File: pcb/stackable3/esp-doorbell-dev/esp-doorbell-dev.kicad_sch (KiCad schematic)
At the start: 26 parts, among them J1 JST XH, J2 Screw_Terminal_01x02, J3 JST XH/PH, J4 JST PH, Q1 BSS84, Q2 BSS84, Q3 BSS84, Q4 2N7002DW, Q5 BSS138, U1 WS2811F, U2 G3MB-202P-5VDC

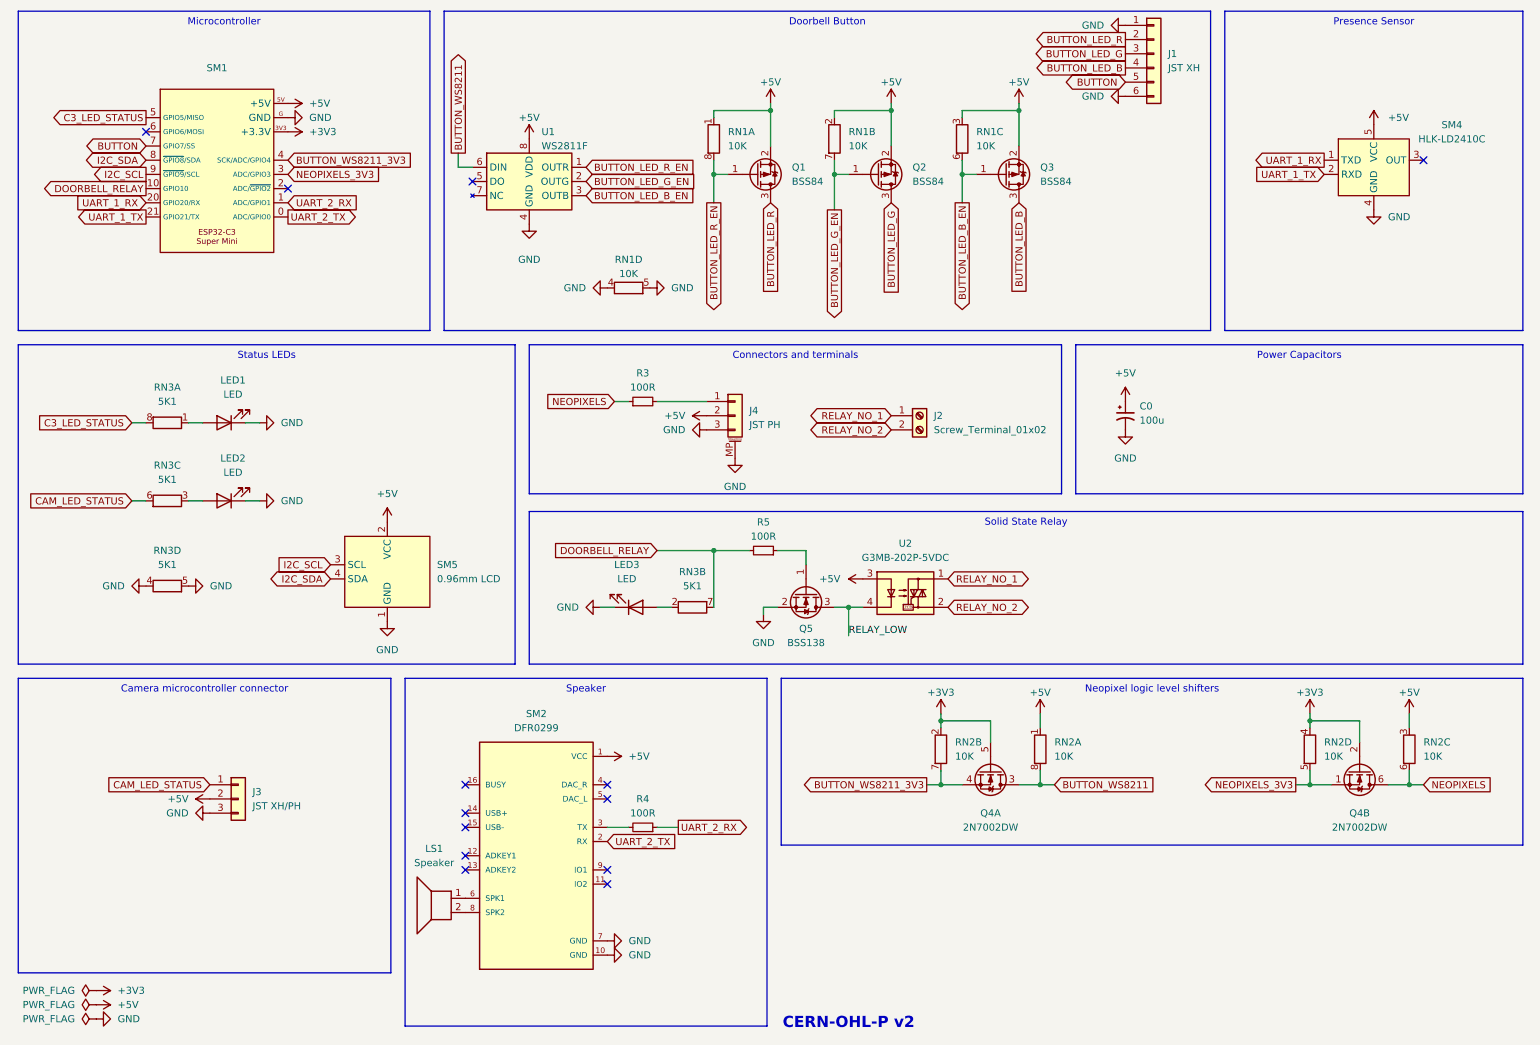
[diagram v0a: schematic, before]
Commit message: Rework misc/esp-doorbell-dev as stackable3/esp-doorbell-dev board
This removes the previous fab outputs for misc/esp-doorbell-dev
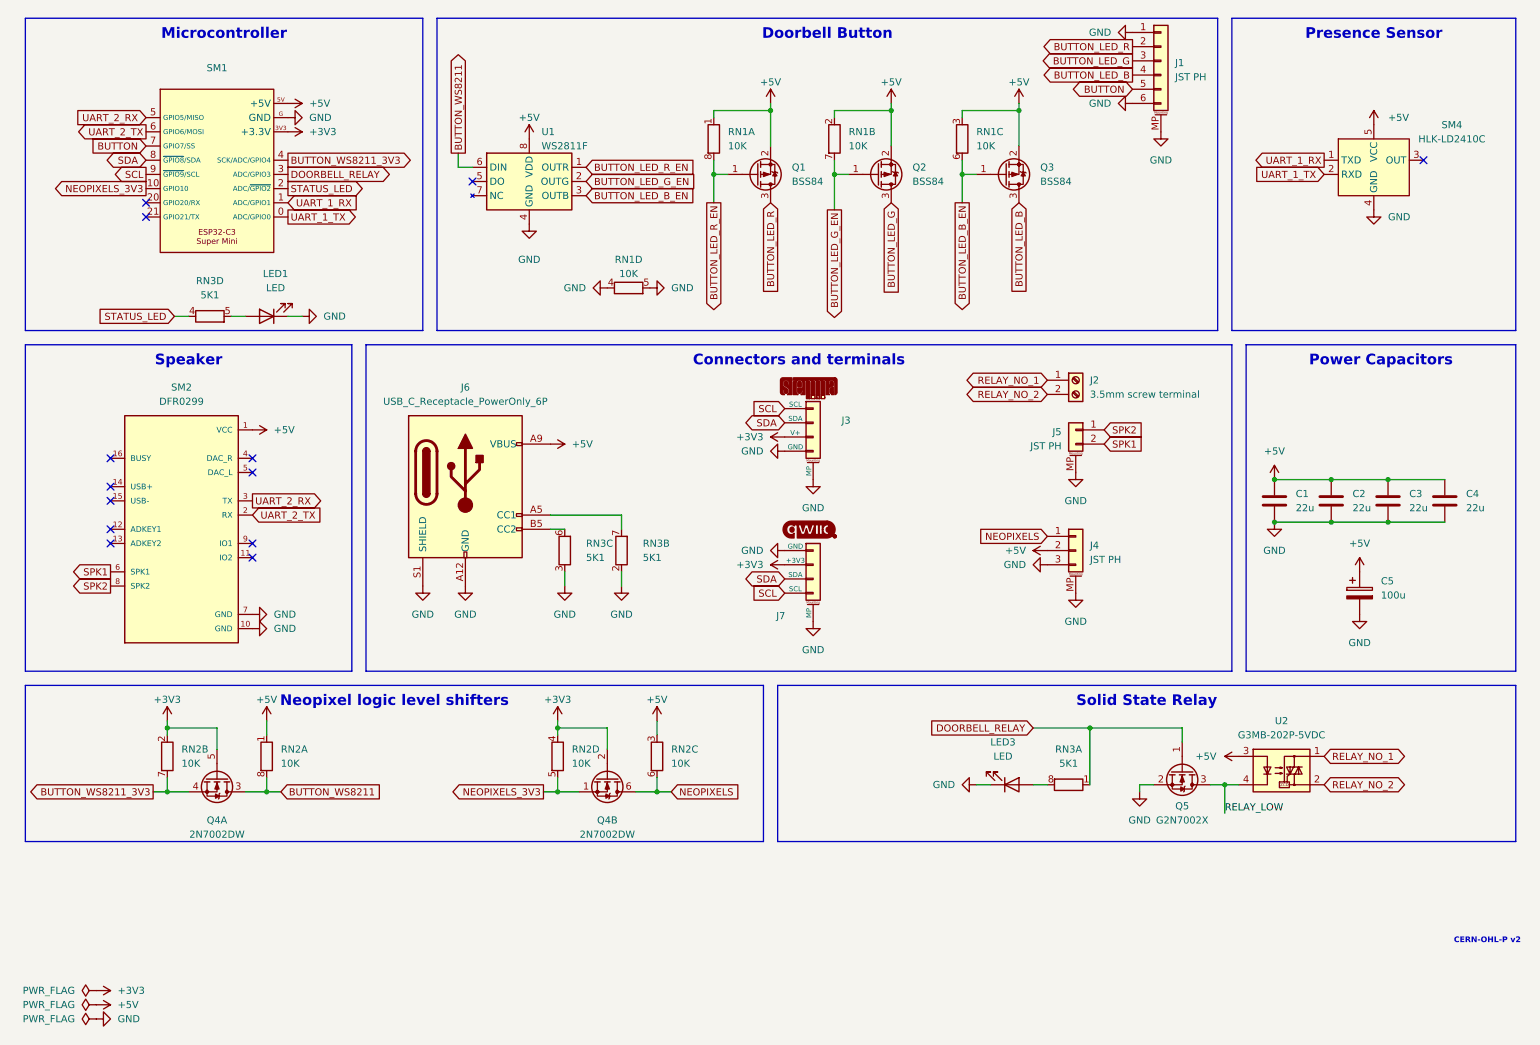
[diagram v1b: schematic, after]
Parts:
- removed C0: 100u, Capacitor_SMD:CP_Elec_5x5.4, symbol Device:C_Polarized_Small_US
- removed J1: JST XH, connector:JST_XH_S6B-XH-2AW_1x06_P2.50mm_Horizontal, symbol Connector_Generic:Conn_01x06
- removed J3: JST XH/PH, custom:Conn_Combo_JST-1x03-XH_PH-THT, symbol Connector_Generic:Conn_01x03
- removed LED2: LED, custom:LED_0603_1608Metric_Pad1.05x0.95mm_HandSolder_simple, symbol Device:LED
- removed LS1: Speaker, custom:Conn_Combo_JST-1x02-XH_PH-SMD-pad2gnd, symbol Device:Speaker
- removed Q5: BSS138, Package_TO_SOT_SMD:SOT-23, symbol Transistor_FET:BSS138
- removed R3, R4, R5: 100R, Resistor_SMD:R_0603_1608Metric_Pad0.98x0.95mm_HandSolder, symbol Device:R_Small
- removed SM5: 0.96mm LCD, module:LCD-OLED-0.96-module-noholes, symbol module:OLED-0.96mm-I2C-module
- added C1, C2, C3, C4: 22u, discrete:C_0603_1608Metric, symbol Device:C
- added C5: 100u, Capacitor_SMD:CP_Elec_5x5.4, symbol Device:C_Polarized
- added J1: JST PH, connector:JST_PH_S6B-PH-SM4-TB_1x06-1MP_P2.00mm_Horizontal, symbol Connector_Generic_MountingPin:Conn_01x06_MountingPin
- added J3: STEMMA, connector:STEMMA-I2C-SMD-horizontal, symbol connector:STEMMA-I2C
- added J5: JST PH, connector:JST_PH_S2B-PH-SM4-TB_1x02-1MP_P2.00mm_Horizontal, symbol Connector_Generic_MountingPin:Conn_01x02_MountingPin
- added J6: USB_C_Receptacle_PowerOnly_6P, connector:USB_C_Receptacle_GCT_USB4125-xx-x_6P_TopMnt_Horizontal_HandSolder, symbol connector:USB_C_Receptacle_PowerOnly_6P_DEALON_009
- added J7: Qwiic, connector:Qwiic-SMD-horizontal-logo, symbol connector:Qwiic
- added Q5: G2N7002X, package:SOT-523, symbol discrete:G2N7002X
- J2: value Screw_Terminal_01x02 -> 3.5mm screw terminal
- RN1, RN2, RN3: footprint Resistor_SMD:R_Array_Convex_4x0603 -> discrete:R_Array_Convex_4x0603_HandSolder
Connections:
- net +3V3: now also J3.3 (V+), J7.2 (+3V3)
- net +5V: now also C1.1, C2.1, C3.1, C4.1, C5.1, J6.A9 (VBUS), J6.B9 (VBUS)
- net BUTTON: now also J1.5 (Pin_5)
- net BUTTON_LED_B: now also J1.4 (Pin_4)
- net BUTTON_LED_G: now also J1.3 (Pin_3)
- net BUTTON_LED_R: now also J1.2 (Pin_2)
- net DOORBELL_RELAY: now also RN3.1 (R1.1), SM1.3 (ADC/GPIO3), Q5.1 (G); no longer RN3.7 (R2.2), SM1.10 (GPIO10)
- net GND: now also RN3.2 (R2.1), RN3.3 (R3.1), C1.2, C2.2, C3.2, C4.2, C5.2, J1.1 (Pin_1), J1.6 (Pin_6), J1.MP (MountPin), J3.4 (GND), J3.MP, J5.MP (MountPin), J6.A12 (GND), J6.B12 (GND), J6.S1 (SHIELD), J7.1 (GND), J7.MP, Q5.2 (S); no longer RN3.4 (R4.1), RN3.5 (R4.2)
- net NEOPIXELS: now also J4.1 (Pin_1)
- net NEOPIXELS_3V3: now also SM1.10 (GPIO10); no longer SM1.3 (ADC/GPIO3)
- net RELAY_LOW: now also Q5.3 (D)
- net UART_1_RX: now also SM1.1 (ADC/GPIO1); no longer SM1.20 (GPIO20/RX)
- net UART_1_TX: now also SM1.0 (ADC/GPIO0); no longer SM1.21 (GPIO21/TX)
- net UART_2_RX: now also SM1.5 (GPIO5/MISO), SM2.3 (TX); no longer SM1.1 (ADC/GPIO1)
- net UART_2_TX: now also SM1.6 (GPIO6/MOSI); no longer SM1.0 (ADC/GPIO0)
- net at LED3.2 (A): now also RN3.8 (R1.2); no longer RN3.2 (R2.1)
- net at LED1.2 (A): now also RN3.5 (R4.2); no longer RN3.1 (R1.1)
- net SPK1: now reaches SM2.6 (SPK1)
- net SPK1: now also J5.2 (Pin_2)
- net SPK2: now reaches SM2.8 (SPK2)
- net SPK2: now also J5.1 (Pin_1)
- net STATUS_LED: now reaches SM1.2 (ADC/~{GPIO2})
- net STATUS_LED: now also RN3.4 (R4.1)
- removed net C3_LED_STATUS: RN3.8 (R1.2), SM1.5 (GPIO5/MISO)
- net CAM_LED_STATUS: no longer names the net of RN3.6 (R3.2)
- net CAM_LED_STATUS: now also J6.B5 (CC2)
- net I2C_SCL renamed SCL
- net SCL: now also J3.1 (SCL), J7.4 (SCL)
- net I2C_SDA renamed SDA
- net SDA: now also J3.2 (SDA), J7.3 (SDA)
- new net: J6.A5 (CC1), RN3.7 (R2.2)
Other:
- moved on the sheet: J2, J4, LED1, LED3, Q4A, Q4B, RN2A, RN2B, RN2C, RN2D, SM2, U2
